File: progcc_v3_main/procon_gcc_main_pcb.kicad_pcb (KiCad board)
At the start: 4 copper layers, 110.9 x 59.5 mm, 110 parts, among them J1 Rumble, J2 Rumble, J3 To Button Board, J4 Conn_01x06_Female, J9 USB_C_Receptacle, Q1 Q_PMOS_GDS, Q2 Q_PMOS_GDS, Q3 Q_PMOS_GDS, Q4 BSS138, Q5 BSS138, Q6 BSS138, SW1 GL18_SW, SW2 GL18_SW, SW3 TS-1187A-B-A-B, T1 36-8730, T2 36-8730, T3 36-8730, T4 36-8730, U1 GH39F (Hall SOT23), U10 MCP3002, U2 GH39F (Hall SOT23), U3 GH39F (Hall SOT23), U4 GH39F (Hall SOT23), U5 GL16112, U6 RP2040, U7 LP3986-33B3F, U8 MCP3002, U9 W25Q128JVS, Y1 Crystal_GND3

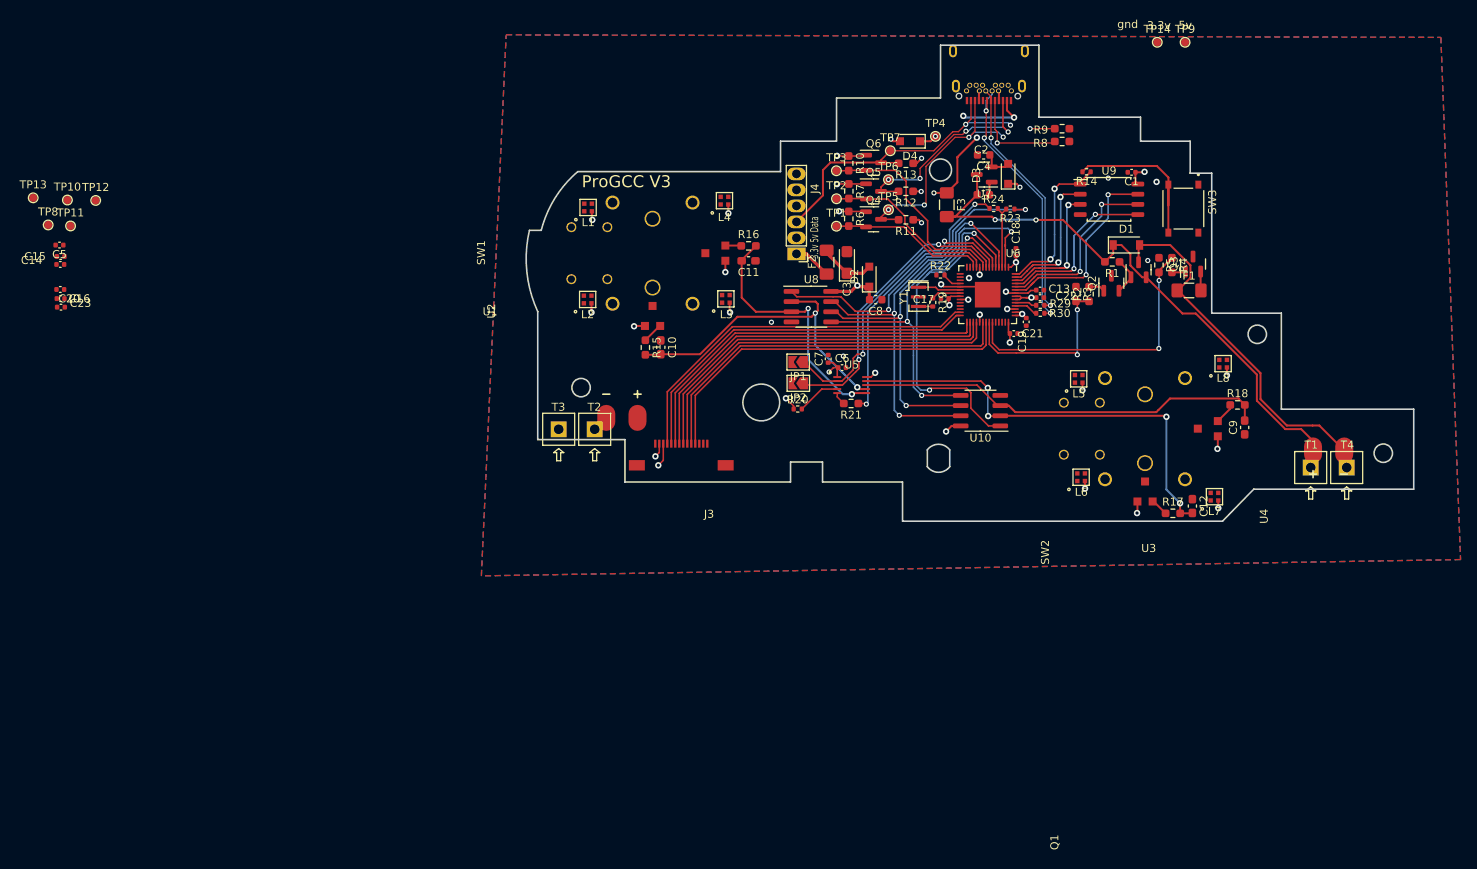
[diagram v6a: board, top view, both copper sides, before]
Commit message: Kicad 7 and Routing
More routing done
Updated to Kicad 7 file types
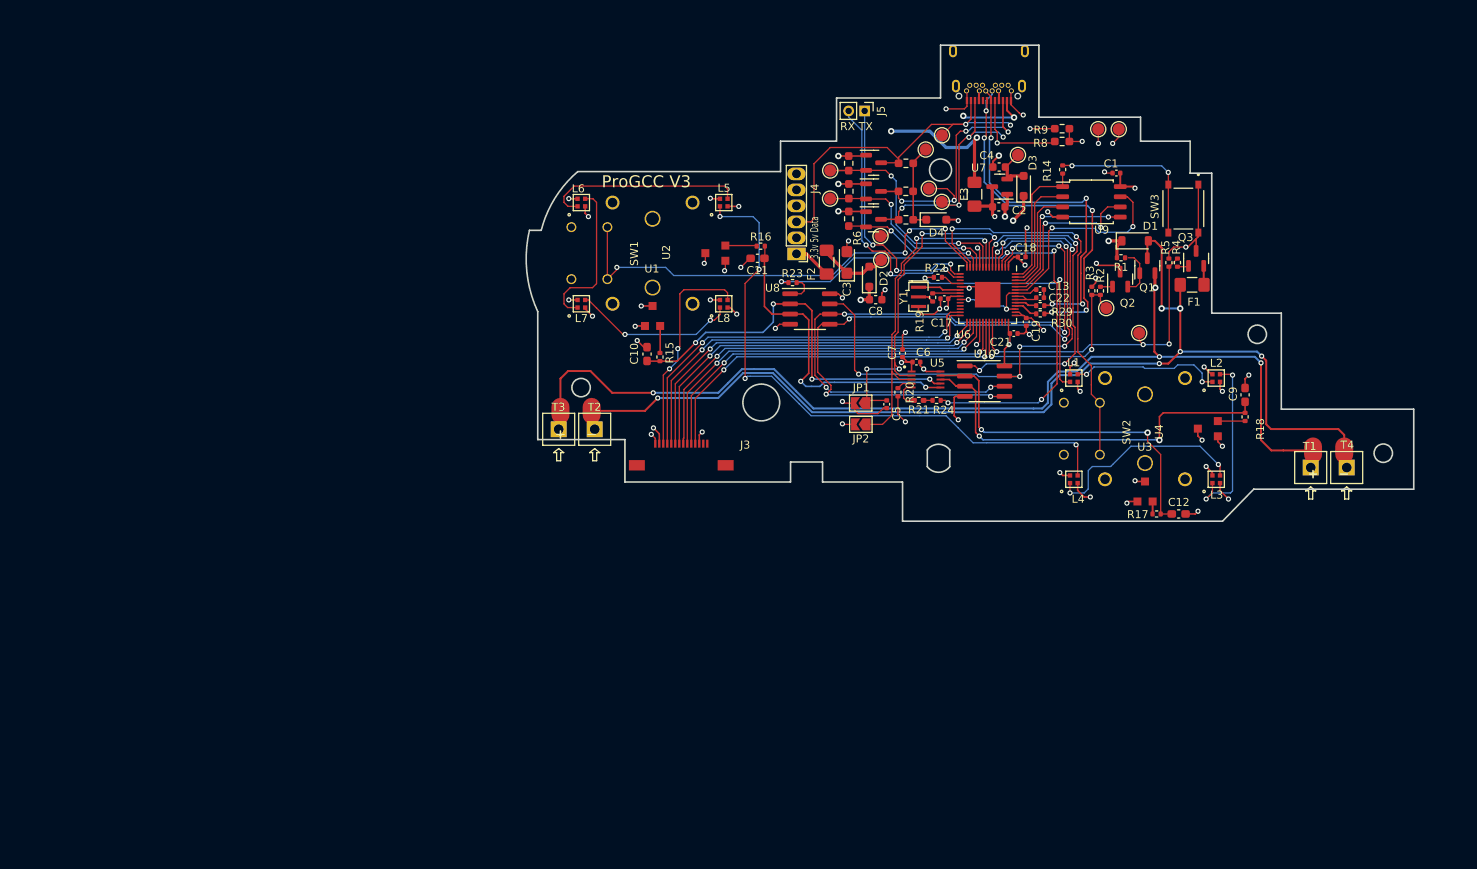
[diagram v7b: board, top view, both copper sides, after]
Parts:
- removed C14, C16, C20, C23: 100n, Capacitor_SMD:C_0402_1005Metric
- removed C15: 1u, Capacitor_SMD:C_0402_1005Metric
- removed TP10: TestPoint, progcc_v3:TestPoint_Pad_D1mm
- added J5: Conn_01x02_Pin, Connector_PinHeader_2.00mm:PinHeader_1x02_P2.00mm_Vertical, F.Cu at (122.9, 100.3)
- J9: footprint procon_gcc:Shou Han Type-C 24P QCHT -> progcc_v3:Shou Han Type-C 24P QCHT
- R1, R15, R16, R17, R18, R2, R3, R4, R5: footprint Resistor_SMD:R_0603_1608Metric_Pad0.98x0.95mm_HandSolder -> Resistor_SMD:R_0402_1005Metric
- R21: footprint Resistor_SMD:R_0603_1608Metric_Pad0.98x0.95mm_HandSolder -> Resistor_SMD:R_0402_1005Metric_Pad0.72x0.64mm_HandSolder
- TP1, TP11, TP12, TP13, TP14, TP2, TP3, TP4, TP5, TP7, TP8, TP9: footprint progcc_v3:TestPoint_Pad_D1mm -> TestPoint:TestPoint_Pad_D1.5mm
- TP6: footprint Heatsink:TestPoint_Pad_D1mm -> TestPoint:TestPoint_Pad_D1.5mm
- moved TP11 134.2 mm to (157.2, 128.1)
- moved TP8 132.7 mm to (153.1, 125.0)
- moved TP13 123.2 mm to (142.1, 105.8)
- moved C5 105.3 mm to (125.7, 137.0), turned to -90 degrees
- moved TP12 98.5 mm to (125.0, 119.0)
- moved L7 82.7 mm to (87.5, 124.4)
- moved L2 79.2 mm to (166.9, 133.7)
- moved L6 71.3 mm to (87.5, 111.8)
- moved L3 65.3 mm to (166.9, 146.4)
- moved L1 64.4 mm to (149.1, 133.7)
- moved L8 62.9 mm to (105.3, 124.4)
- moved L4 55.9 mm to (149.1, 146.4)
- moved L5 49.5 mm to (105.3, 111.8)
- moved R23 28.7 mm to (113.9, 121.8)
- moved R24 25.0 mm to (131.9, 136.5)
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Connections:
- C5 pad 1: GULI_DAT -> GULI_CALIBRATE
- U6 pad 13: unconnected-(U6-Pad13) -> RS_BUTTON
- U6 pad 14: unconnected-(U6-Pad14) -> LS_BUTTON
- U6 pad 15: unconnected-(U6-Pad15) -> UART0_TX
- U6 pad 16: unconnected-(U6-Pad16) -> UART0_RX
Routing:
- net +5V: track 72.2 -> 186.8 mm, vias 2 -> 7
- net RUMBLE-: track 47.5 -> 143.3 mm, vias 0 -> 6
- net GND: track 9.41 -> 104.6 mm, vias 8 -> 40
- net SR_RGB: track 0.00 -> 75.6 mm, vias 0 -> 4
- net GPIO1: track 8.24 -> 71.2 mm, vias 0 -> 5
- net LS_BUTTON: track 0.00 -> 59.6 mm, vias 0 -> 4
- net RS_BUTTON: track 0.00 -> 50.4 mm, vias 0 -> 2
- net P_RX: track 46.2 -> 87.6 mm, vias 3 -> 6
- net P_LCS: track 39.2 -> 3.71 mm, vias 2 -> 0
- net GULI_TXD: track 34.8 -> 1.12 mm, vias 2 -> 0
- net UART0_RX: track 0.00 -> 33.0 mm, vias 0 -> 3
- net SL_RGB: track 0.00 -> 32.3 mm, vias 0 -> 2
- net UART0_TX: track 0.00 -> 31.6 mm, vias 0 -> 3
- net P_TX: track 53.8 -> 84.1 mm, vias 3 -> 6
- net Net-(L3-DOUT): track 0.00 -> 25.9 mm, vias 0 -> 2
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- added copper zone on In2.Cu, net +3V3
- added copper zone on In1.Cu, net GND
- removed copper zone on In1.Cu, net +3V3
- removed copper zone on B.Cu, net GND
- removed copper zone on F.Cu, net GND
- removed copper zone on In2.Cu, net GND
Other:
- rule solder_mask_min_width: 0.25 -> 0.22
- board text added: "RX TX"
- board text removed: "3.3v"
- board text removed: "5v"
- board text removed: "gnd"
